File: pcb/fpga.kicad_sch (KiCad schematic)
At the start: 21 parts, among them J12 MEM_WR_RD_J, J13 KB, J5 FPGA JTAG, J7 RAM cacheable, J8 ROM cacheable, U2 XC2S100TQ144, Y1 TXC-7C, Y2 GTXO-14T

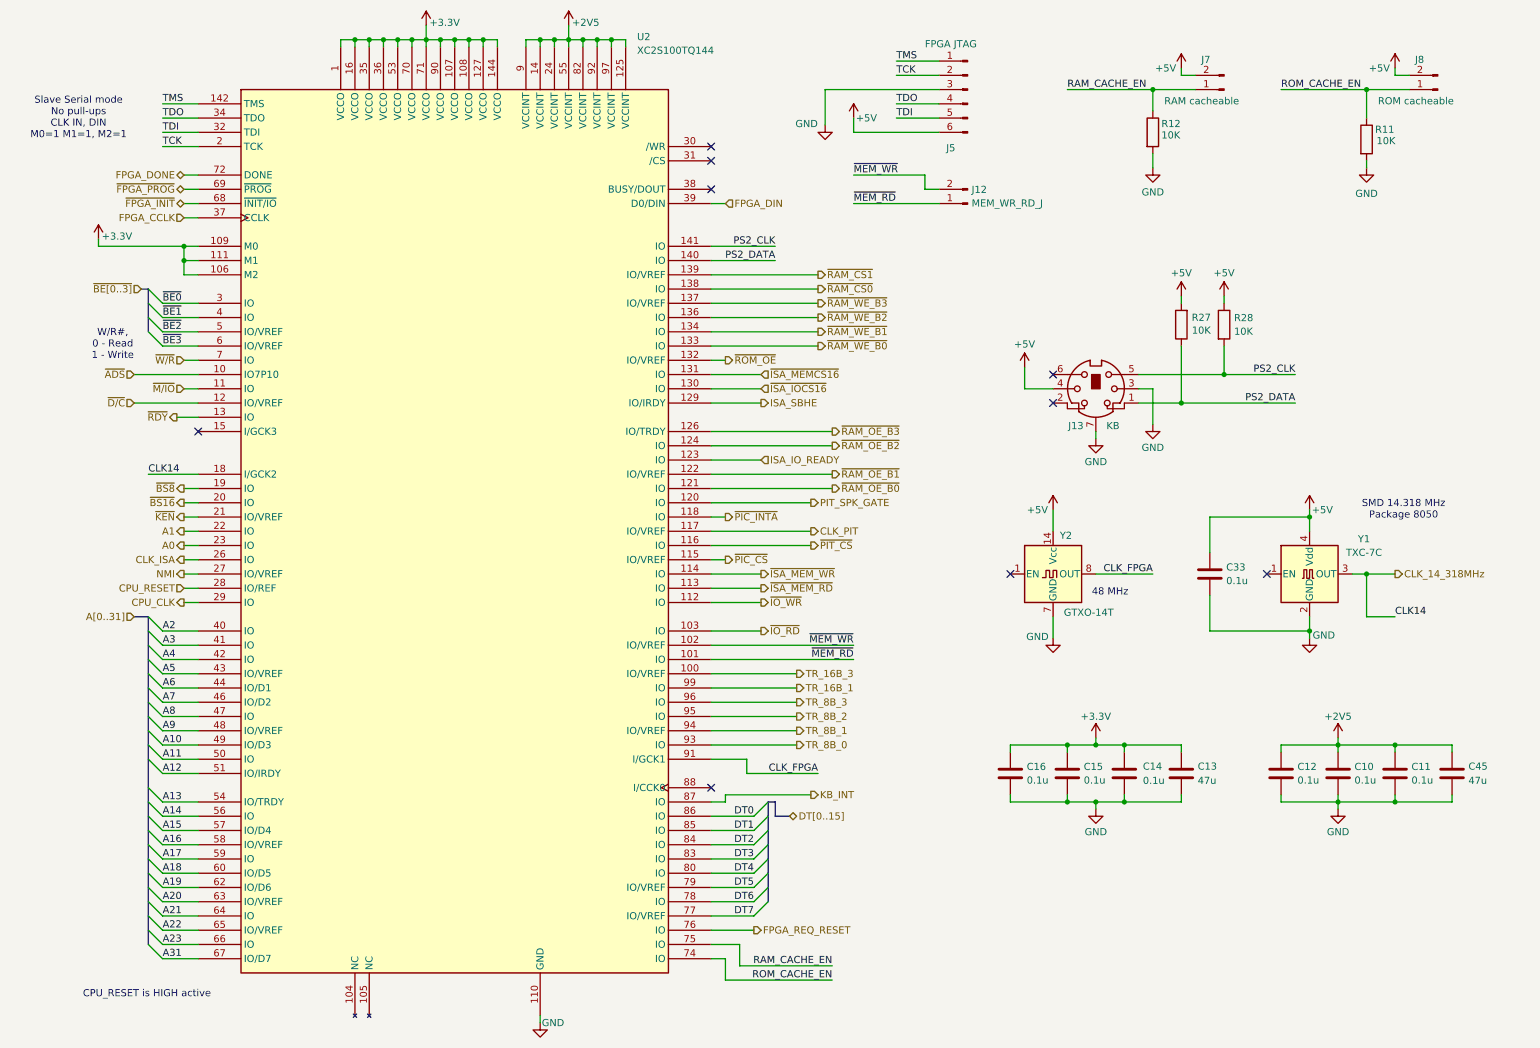
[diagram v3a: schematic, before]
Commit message: removing unused functionality J12 MEM_WR MEM_RD (and corresponding MUX_MEM_WR MUX_MEM_RD vhdl), moving A0 pin 23->101, A1 22->102, freeing pins 22 23
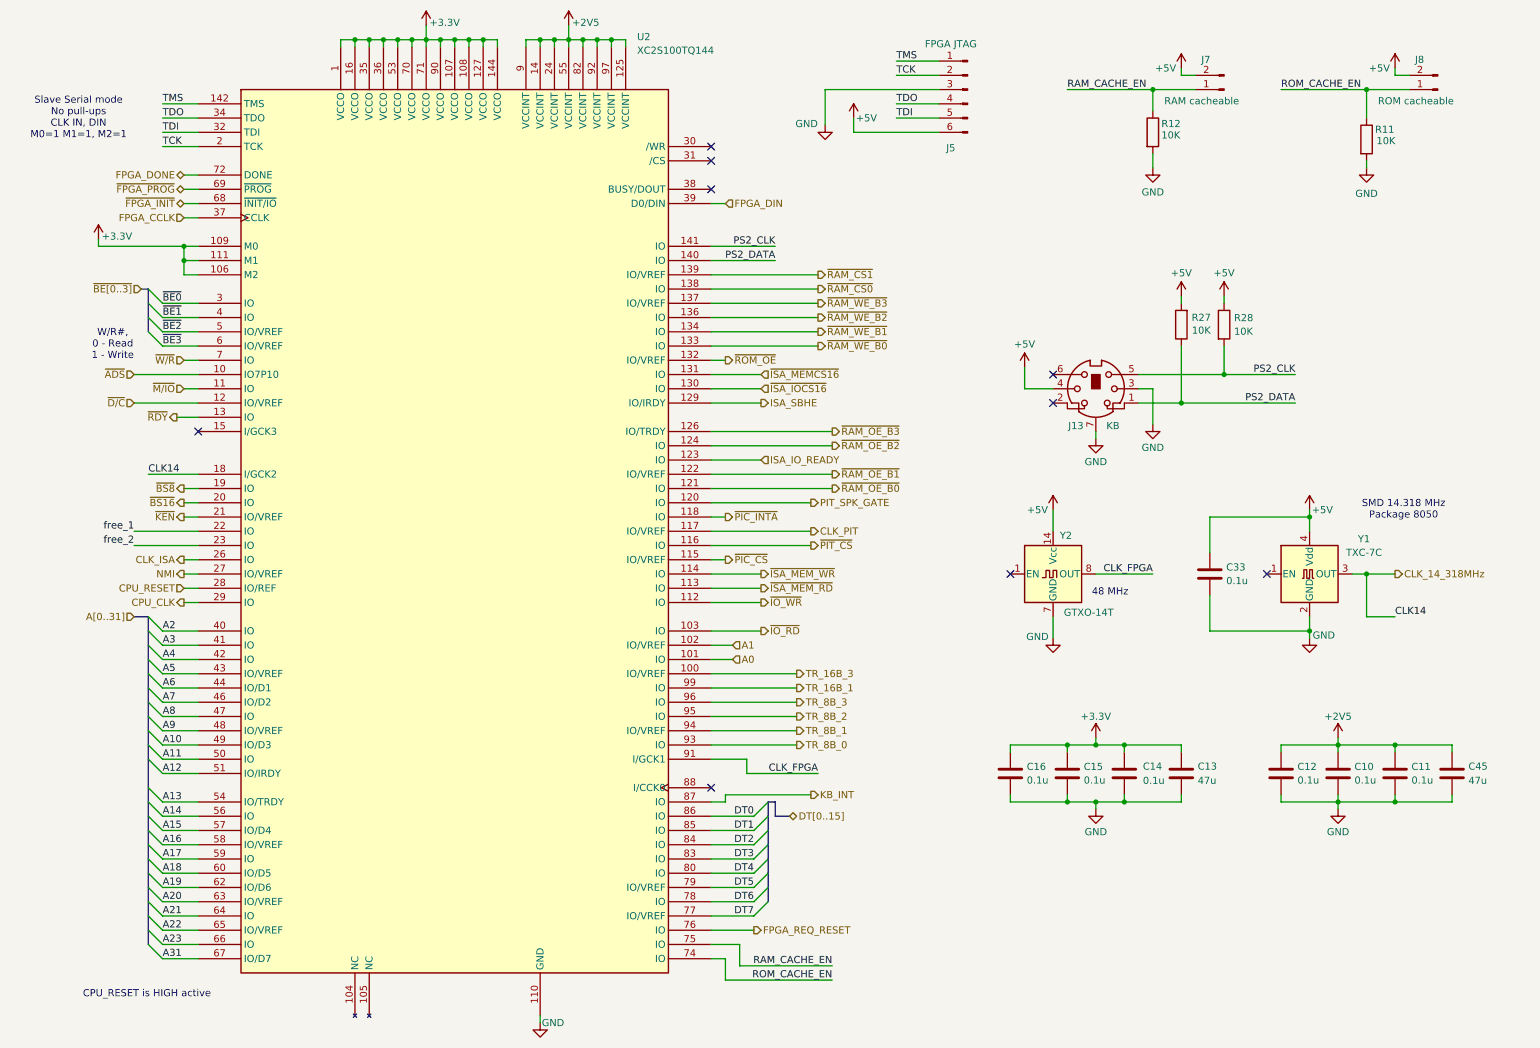
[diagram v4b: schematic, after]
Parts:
- removed J12: MEM_WR_RD_J, Connector_PinHeader_2.54mm:PinHeader_1x02_P2.54mm_Vertical, symbol Connector:Conn_01x02_Pin
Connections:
- net ~{MEM_RD} is gone; now on net A0: U2.101 (IO)
- net ~{MEM_WR} is gone; now on net A1: U2.102 (IO/VREF)
- net A0: no longer U2.23 (IO)
- net A1: no longer U2.22 (IO)
- new net free_1: U2.22 (IO)
- new net free_2: U2.23 (IO)
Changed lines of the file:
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@@
 		)
 	)
-	(wire
-		(pts
-			(xy 165.1 43.18) (xy 177.8 43.18)
-		)
-		(stroke
-			(width 0)
-			(type default)
-		)
-	)
 	(bus
 		(pts
@@
 	(wire
 		(pts
+			(xy 139.7 129.54) (xy 143.51 129.54)
+		)
+		(stroke
+			(width 0)
+			(type default)
+		)
+	)
+	(wire
+		(pts
 			(xy 208.28 154.94) (xy 208.28 156.21)
 		)
@@
 	(wire
 		(pts
-			(xy 165.1 48.26) (xy 180.34 48.26)
-		)
-		(stroke
-			(width 0)
-			(type default)
-		)
-	)
-	(wire
-		(pts
 			(xy 109.22 193.04) (xy 109.22 194.31)
 		)
@@
 	(wire
 		(pts
-			(xy 177.8 45.72) (xy 180.34 45.72)
-		)
-		(stroke
-			(width 0)
-			(type default)
-		)
-	)
-	(wire
-		(pts
 			(xy 41.91 154.94) (xy 48.26 154.94)
 		)
@@
 		)
 	)
-	(wire
-		(pts
-			(xy 177.8 43.18) (xy 177.8 45.72)
-		)
-		(stroke
-			(width 0)
-			(type default)
-		)
-	)
 	(bus
 		(pts
@@
 	(wire
 		(pts
-			(xy 45.72 106.68) (xy 48.26 106.68)
-		)
-		(stroke
-			(width 0)
-			(type default)
-		)
-	)
-	(wire
-		(pts
 			(xy 208.28 144.78) (xy 203.2 144.78)
 		)
@@
 	(wire
 		(pts
-			(xy 139.7 129.54) (xy 165.1 129.54)
-		)
-		(stroke
-			(width 0)
-			(type default)
-		)
-	)
-	(wire
-		(pts
 			(xy 41.91 73.66) (xy 48.26 73.66)
 		)
@@
 	(wire
 		(pts
+			(xy 36.83 106.68) (xy 48.26 106.68)
+		)
+		(stroke
+			(width 0)
+			(type default)
+		)
+	)
+	(wire
+		(pts
 			(xy 142.24 186.69) (xy 161.29 186.69)
 		)
@@
 	(wire
 		(pts
-			(xy 45.72 109.22) (xy 48.26 109.22)
+			(xy 36.83 109.22) (xy 48.26 109.22)
 		)
 		(stroke
@@
 	(wire
 		(pts
+			(xy 139.7 127) (xy 143.51 127)
+		)
+		(stroke
+			(width 0)
+			(type default)
+		)
+	)
+	(wire
+		(pts
 			(xy 139.7 63.5) (xy 158.75 63.5)
 		)
@@
 	(wire
 		(pts
-			(xy 139.7 127) (xy 165.1 127)
-		)
-		(stroke
-			(width 0)
-			(type default)
-		)
-	)
-	(wire
-		(pts
 			(xy 139.7 109.22) (xy 157.48 109.22)
 		)
@@
 		)
 	)
-	(label "~{MEM_WR}"
-		(at 165.1 127 180)
-		(effects
-			(font
-				(size 1.27 1.27)
-			)
-			(justify right bottom)
-		)
-	)
 	(label "A17"
 		(at 41.91 165.1 0)
@@
 		)
 	)
+	(label "free_2"
+		(at 36.83 109.22 180)
+		(effects
+			(font
+				(size 1.27 1.27)
+			)
+			(justify right bottom)
+		)
+	)
 	(label "PS2_DATA"
 		(at 243.84 83.82 180)
@@
 		)
 	)
-	(label "~{MEM_WR}"
-		(at 165.1 43.18 0)
-		(effects
-			(font
-				(size 1.27 1.27)
-			)
-			(justify left bottom)
-		)
-	)
-	(label "~{MEM_RD}"
-		(at 165.1 129.54 180)
-		(effects
-			(font
-				(size 1.27 1.27)
-			)
-			(justify right bottom)
-		)
-	)
 	(label "ROM_CACHE_EN"
 		(at 161.29 186.69 180)
@@
 		)
 	)
-	(label "~{MEM_RD}"
-		(at 165.1 48.26 0)
-		(effects
-			(font
-				(size 1.27 1.27)
-			)
-			(justify left bottom)
-		)
-	)
 	(label "~{BE2}"
 		(at 41.91 71.12 0)
@@
 		)
 	)
+	(label "free_1"
+		(at 36.83 106.68 180)
+		(effects
+			(font
+				(size 1.27 1.27)
+			)
+			(justify right bottom)
+		)
+	)
 	(label "A16"
 		(at 41.91 162.56 0)
@@
 		)
 	)
-	(hierarchical_label "A1"
-		(shape output)
-		(at 45.72 106.68 180)
-		(effects
-			(font
-				(size 1.27 1.27)
-			)
-			(justify right)
-		)
-	)
 	(hierarchical_label "TR_16B_1"
 		(shape output)
@@
 		)
 	)
+	(hierarchical_label "A0"
+		(shape input)
+		(at 143.51 129.54 0)
+		(effects
+			(font
+				(size 1.27 1.27)
+			)
+			(justify left)
+		)
+	)
 	(hierarchical_label "DT[0..15]"
 		(shape bidirectional)
@@
 		)
 	)
-	(hierarchical_label "~{BS8}"
-		(shape output)
-		(at 45.72 99.06 180)
+	(hierarchical_label "A1"
+		(shape input)
+		(at 143.51 127 0)
 		(effects
 			(font
 				(size 1.27 1.27)
 			)
-			(justify right)
+			(justify left)
 		)
 	)
-	(hierarchical_label "A0"
+	(hierarchical_label "~{BS8}"
 		(shape output)
-		(at 45.72 109.22 180)
+		(at 45.72 99.06 180)
 		(effects
 			(font
@@
 					(unit 1)
 				)
-			)
-		)
-	)
-	(symbol
-		(lib_id "Connector:Conn_01x02_Pin")
-		(at 185.42 48.26 180)
-		(unit 1)
-		(exclude_from_sim no)
-		(in_bom yes)
-		(on_board yes)
-		(dnp no)
-		(fields_autoplaced yes)
-		(property "Reference" "J12"
-			(at 186.1312 45.7778 0)
-			(effects
-				(font
-					(size 1.27 1.27)
-				)
-				(justify right)
-			)
-		)
-		(property "Value" "MEM_WR_RD_J"
-			(at 186.1312 48.2021 0)
-			(effects
-				(font
-					(size 1.27 1.27)
-				)
-				(justify right)
-			)
-		)
-		(property "Footprint" "Connector_PinHeader_2.54mm:PinHeader_1x02_P2.54mm_Vertical"
-			(at 185.42 48.26 0)
-			(effects
-				(font
-					(size 1.27 1.27)
-				)
-				(hide yes)
-			)
-		)
-		(property "Datasheet" "~"
-			(at 185.42 48.26 0)
-			(effects
-				(font
-					(size 1.27 1.27)
-				)
-				(hide yes)
-			)
-		)
-		(property "Description" "Generic connector, single row, 01x02, script generated"
-			(at 185.42 48.26 0)
-			(effects
-				(font
-					(size 1.27 1.27)
-				)
-				(hide yes)
-			)
-		)
-		(pin "2"
-		)
-		(pin "1"
-		)
-		(instances
-			(project "homebrew_486"
-				(path "/360fb3b9-a21a-4226-8954-bf45cf17bb35/49c3128c-49f0-451c-bde3-bf7412e8a8c9"
-					(reference "J12")
-					(unit 1)
-				)

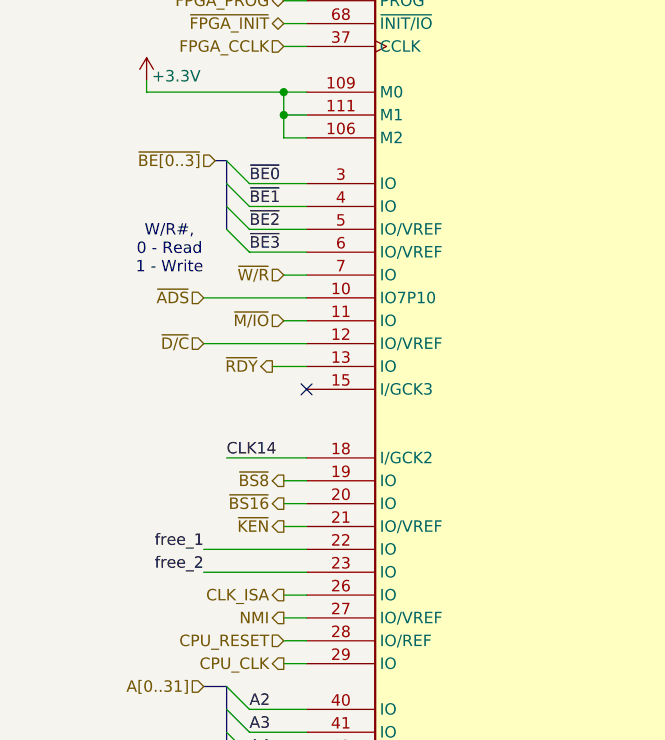
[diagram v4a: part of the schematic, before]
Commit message: reversed BEx FPGA pin order, previous patch also changed CLKMUL jumper to 2 pole
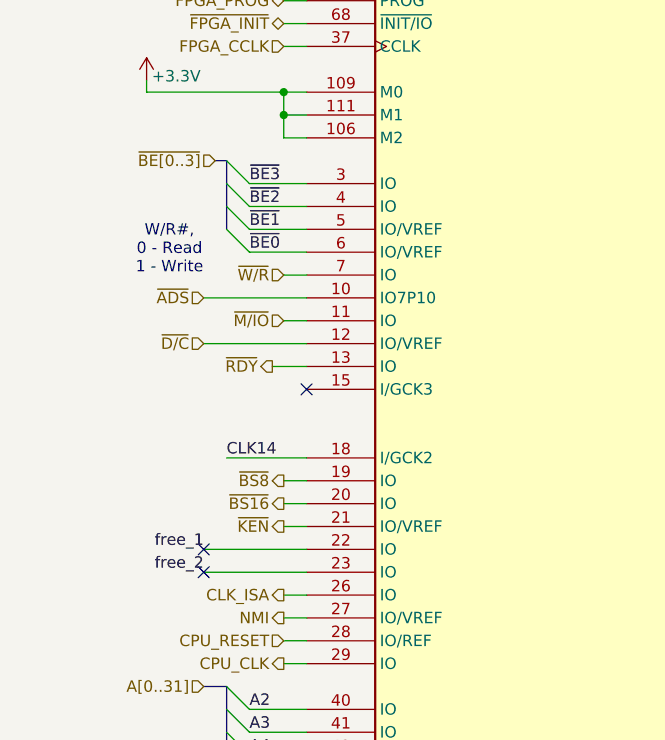
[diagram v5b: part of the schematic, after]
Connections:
- net ~{BE0}: now also U2.6 (IO/VREF); no longer U2.3 (IO)
- net ~{BE1}: now also U2.5 (IO/VREF); no longer U2.4 (IO)
- net ~{BE2}: now also U2.4 (IO); no longer U2.5 (IO/VREF)
- net ~{BE3}: now also U2.3 (IO); no longer U2.6 (IO/VREF)
- no-connect marks 9 -> 11
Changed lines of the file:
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@@
 	)
 	(no_connect
+		(at 36.83 109.22)
+	)
+	(no_connect
 		(at 238.76 114.3)
 	)
@@
 	)
 	(no_connect
+		(at 36.83 106.68)
+	)
+	(no_connect
 		(at 200.66 83.82)
 	)
@@
 		)
 	)
-	(label "~{BE1}"
-		(at 41.91 68.58 0)
-		(effects
-			(font
-				(size 1.27 1.27)
-			)
-			(justify left bottom)
-		)
-	)
 	(label "TDI"
 		(at 41.91 35.56 0)
@@
 		)
 	)
-	(label "~{BE0}"
-		(at 41.91 66.04 0)
-		(effects
-			(font
-				(size 1.27 1.27)
-			)
-			(justify left bottom)
-		)
-	)
 	(label "A20"
 		(at 41.91 172.72 0)
@@
 		)
 	)
+	(label "~{BE3}"
+		(at 41.91 66.04 0)
+		(effects
+			(font
+				(size 1.27 1.27)
+			)
+			(justify left bottom)
+		)
+	)
 	(label "DT0"
 		(at 147.32 157.48 180)
@@
 		)
 	)
+	(label "~{BE0}"
+		(at 41.91 73.66 0)
+		(effects
+			(font
+				(size 1.27 1.27)
+			)
+			(justify left bottom)
+		)
+	)
 	(label "ROM_CACHE_EN"
 		(at 161.29 186.69 180)
@@
 		)
 	)
+	(label "~{BE1}"
+		(at 41.91 71.12 0)
+		(effects
+			(font
+				(size 1.27 1.27)
+			)
+			(justify left bottom)
+		)
+	)
 	(label "A21"
 		(at 41.91 175.26 0)
@@
 	)
 	(label "~{BE2}"
-		(at 41.91 71.12 0)
+		(at 41.91 68.58 0)
 		(effects
 			(font
@@
 		(effects
 			(font
-				(size 1.27 1.27)
-			)
-			(justify left bottom)
-		)
-	)
-	(label "~{BE3}"
-		(at 41.91 73.66 0)
-		(effects
-			(font
